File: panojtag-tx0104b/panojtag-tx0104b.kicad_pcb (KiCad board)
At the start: 2 copper layers, 18 x 18 mm, 9 parts, among them J1 Conn_01x06, J2 Conn_01x06, U1 TXB0104D

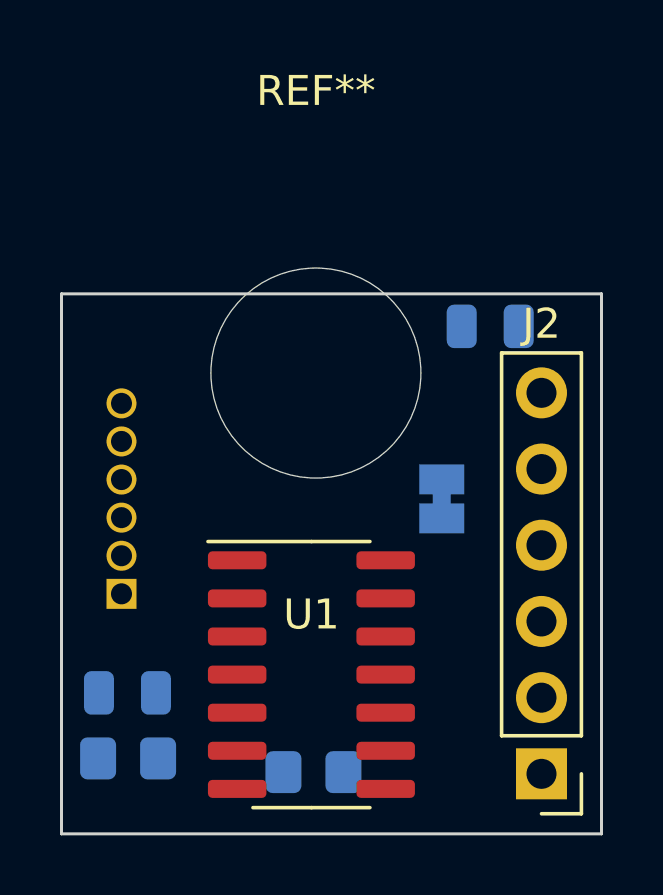
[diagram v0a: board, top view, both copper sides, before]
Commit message: Cleaned up and routed TX0104B version, but e're not going to use it. Routed using TopoR with 45deg tracks.
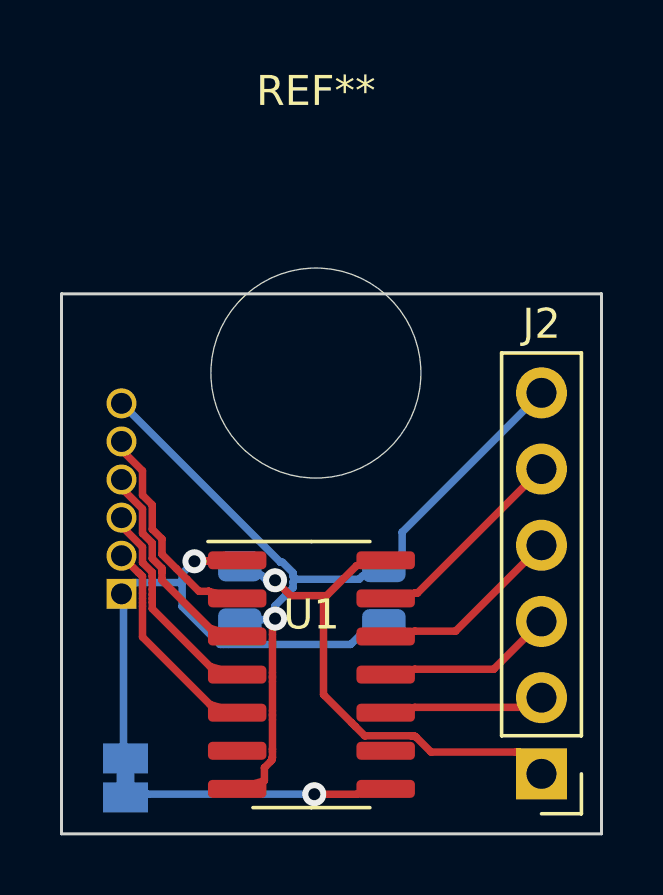
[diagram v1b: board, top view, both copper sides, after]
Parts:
- removed R1, R2: 100K, Resistor_SMD:R_0805_2012Metric_Pad1.20x1.40mm_HandSolder
- moved JP1 14.1 mm to (76.3, 86.1), turned to -90 degrees
- moved C1 9.65 mm to (84.9, 80.0), turned to 90 degrees
- moved C2 4.97 mm to (80.1, 80.0), turned to -90 degrees
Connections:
- JP1 pad 2: /Vcc -> Net-(JP1-Pad2)
- U1 pad 8: /Vcc -> Net-(JP1-Pad2)
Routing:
- net GND: track 0.00 -> 28.7 mm, vias 0 -> 1
- net /Vcc: track 0.00 -> 18.2 mm, vias 0 -> 1
- net /Vref: track 0.00 -> 17.3 mm, vias 0 -> 1
- net Net-(JP1-Pad2): track 0.00 -> 8.70 mm, vias 0 -> 1
- net /A_TCK: track 0.00 -> 7.37 mm
- net /A_TDI: track 0.00 -> 7.13 mm
- net /A_TMS: track 0.00 -> 7.13 mm
- net /A_TDO: track 0.00 -> 7.13 mm
- net /B_TCK: track 0.00 -> 6.92 mm
- net /B_TDO: track 0.00 -> 6.40 mm
- net /B_TMS: track 0.00 -> 5.87 mm
- net /B_TDI: track 0.00 -> 5.34 mm
